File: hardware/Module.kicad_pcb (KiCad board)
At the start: 2 copper layers, 47.6 x 220.4 mm, 124 parts, among them J1 Jack, J10 Jack, J11 Jack, J12 Jack, J13 Micro_SD, J14 NW_B, J15 Jack, J16 Jack, J17 Power, J18 Jack, J19 Jack, J2 OLED, J20 SW_B, J21 NW_A, J22 SW_A, J23 NE_A, J3 NE_B, J4 Jack, J5 Jack, J6 Jack, J7 Jack, J8 Jack, J9 Jack, SW1 Encoder, U1 TL074, U2 TL074, U3 TL074, U4 MCP6004, U5 MCP6002, U7 LM4040C10

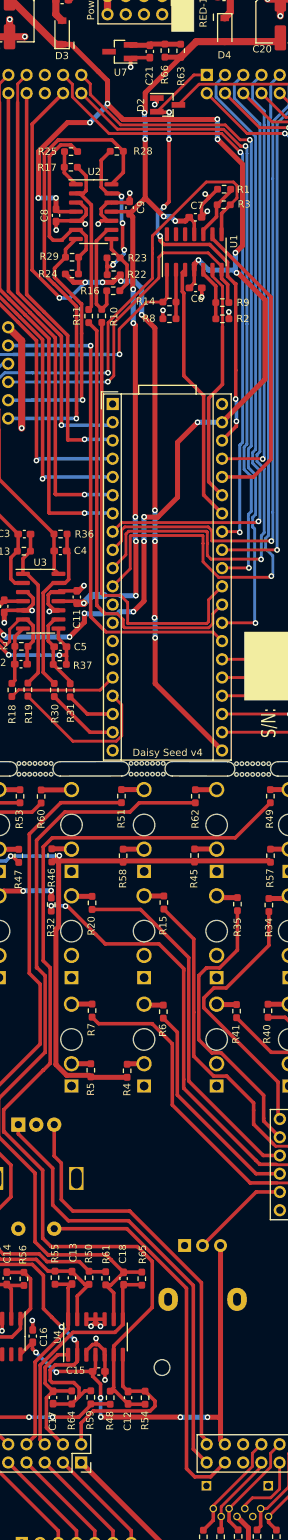
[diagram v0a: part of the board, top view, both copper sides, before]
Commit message: Connect -10V between boards
Signed-off-by: Petr Horacek <hrck@protonmail.com>
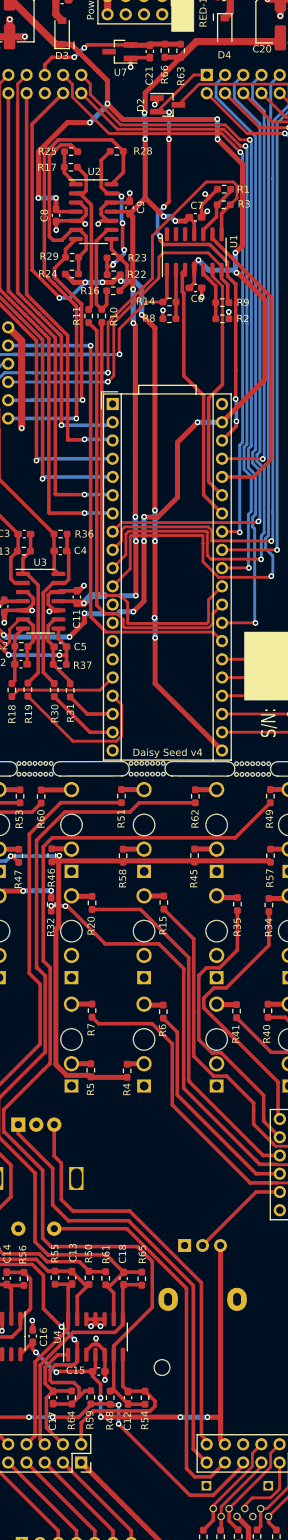
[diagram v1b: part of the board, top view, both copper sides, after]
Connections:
- J14 pad 7: unconnected-(J14-Pad7) -> -10V
- J21 pad 7: unconnected-(J21-Pad7) -> -10V
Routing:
- net -10V: track 66.2 -> 108.2 mm, vias 5 -> 9

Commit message: Release version 0.6.0
Signed-off-by: Petr Horacek <hrck@protonmail.com>
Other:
- board text added: "board v0.6.0"
- board text removed: "board v0.5.0"
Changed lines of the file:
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@@
     (title "Proton")
     (date "2022-03-06")
-    (rev "v0.5.0")
+    (rev "v0.6.0")
     (company "Petr Horáček")
     (comment 1 "petr@zlosynth.com")
@@
     (effects (font (size 1 1) (thickness 0.15)))
   )
-  (gr_text "board v0.5.0" (at 131.978677 50.246953 90) (layer "F.SilkS")
+  (gr_text "board v0.6.0" (at 131.978677 50.246953 90) (layer "F.SilkS")
     (effects (font (size 1 1) (thickness 0.15)) (justify left))
   )
